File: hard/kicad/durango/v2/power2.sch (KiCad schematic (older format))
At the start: 71 parts, among them J11 EXPANSION, J4 LED, J605 COMPONENT VIDEO, J7 POWER IN, J706 COMPOSITE, J8 DEBUG, J9 CARTRIDGE, Q608 BC548, Q609 BC548, Q610 BC548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

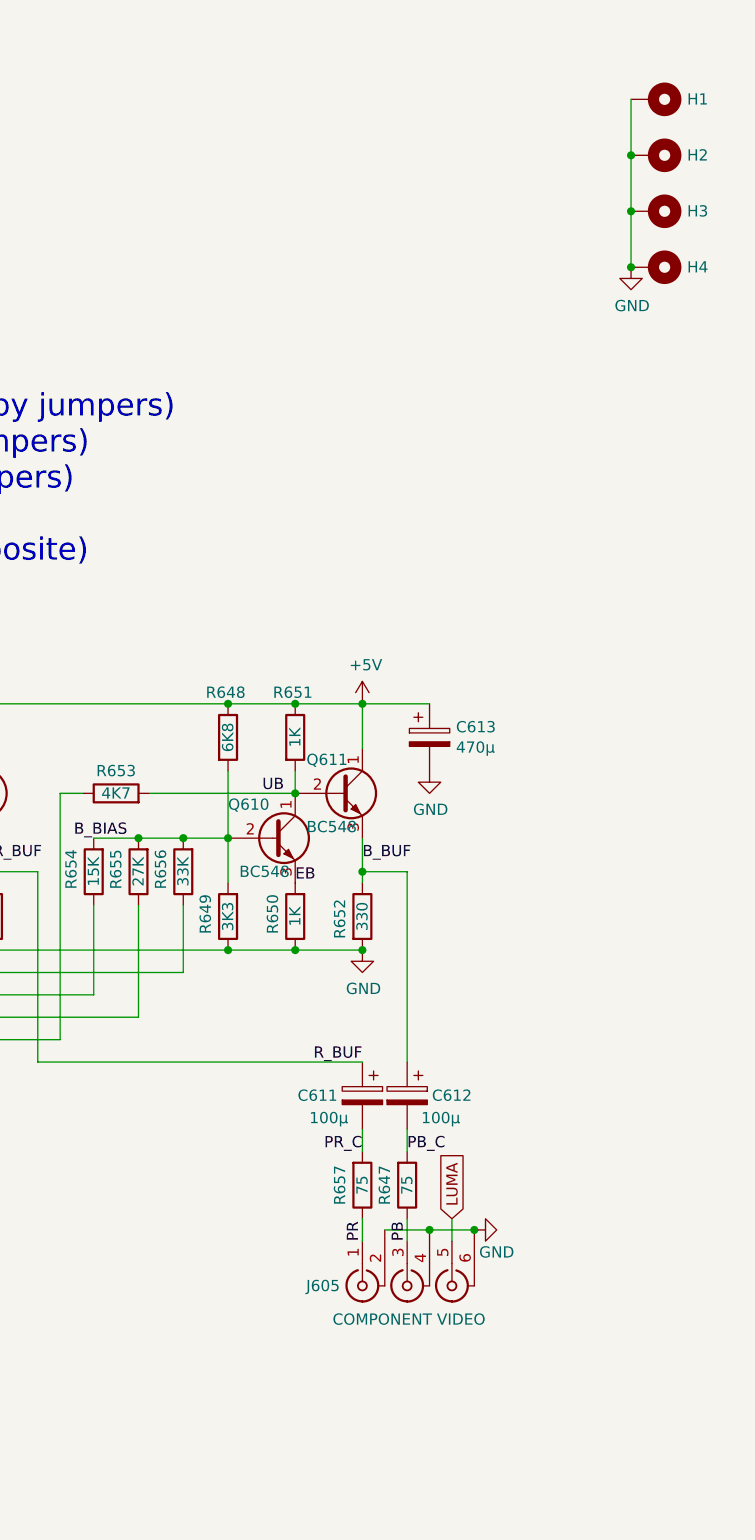
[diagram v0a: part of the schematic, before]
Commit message: add narrow SRAM footprint
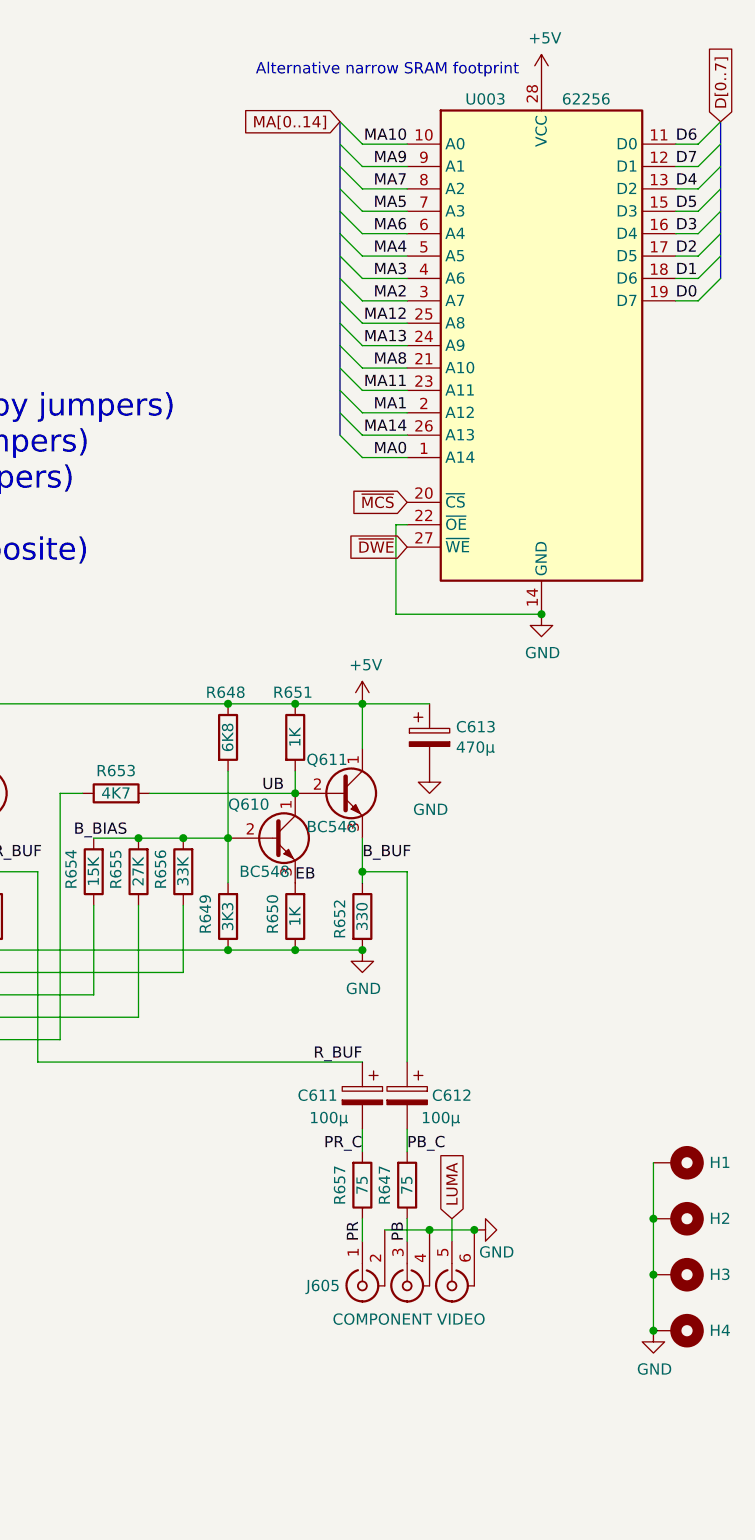
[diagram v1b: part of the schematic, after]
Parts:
- added U003: 62256, Package_DIP:DIP-28_W7.62mm_Socket, symbol 62256:62256
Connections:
- net +5V: now also U003.28 (VCC)
- net D0: now also U003.19 (D7)
- net D1: now also U003.18 (D6)
- net D2: now also U003.17 (D5)
- net D3: now also U003.16 (D4)
- net D4: now also U003.13 (D2)
- net D5: now also U003.15 (D3)
- net D6: now also U003.11 (D0)
- net D7: now also U003.12 (D1)
- net GND: now also U003.14 (GND), U003.22 (~OE~)
- new net MA0: U003.1 (A14)
- new net MA1: U003.2 (A12)
- new net MA10: U003.10 (A0)
- new net MA11: U003.23 (A11)
- new net MA12: U003.25 (A8)
- new net MA13: U003.24 (A9)
- new net MA14: U003.26 (A13)
- new net MA2: U003.3 (A7)
- new net MA3: U003.4 (A6)
- new net MA4: U003.5 (A5)
- new net MA5: U003.7 (A3)
- new net MA6: U003.6 (A4)
- new net MA7: U003.8 (A2)
- new net MA8: U003.21 (A10)
- new net MA9: U003.9 (A1)
- new net ~DWE: U003.27 (~WE~)
- new net ~MCS: U003.20 (~CS)
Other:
- note added: "Alternative narrow SRAM footprint"
- moved on the sheet: H1, H2, H3, H4

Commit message: fix CCIR v2.2
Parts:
- JP3: value SWITCH -> POWER
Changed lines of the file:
@@
 P 2600 6500
 F 0 "R32" H 2670 6546 50  0000 L CNN
-F 1 "1K" V 2600 6450 50  0000 L CNN
+F 1 "1K" V 2600 6450 50  0000 L CIN
 F 2 "Resistor_THT:R_Axial_DIN0207_L6.3mm_D2.5mm_P2.54mm_Vertical" V 2530 6500 50  0001 C CNN
 F 3 "~" H 2600 6500 50  0001 C CNN
@@
 P 1400 800
 F 0 "JP3" V 1250 600 50  0000 L CNN
-F 1 "SWITCH" H 1300 900 50  0000 L CNN
+F 1 "POWER" H 1300 900 50  0000 L CNN
 F 2 "durango:PowerSwitch" H 1400 800 50  0001 C CNN
 F 3 "~" H 1400 800 50  0001 C CNN

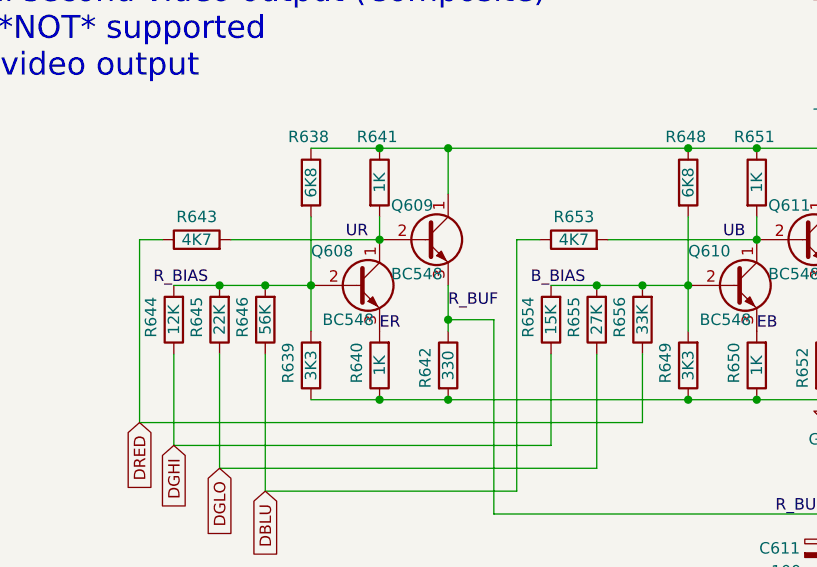
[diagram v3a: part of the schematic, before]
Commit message: fix YUV output values on silkscreen
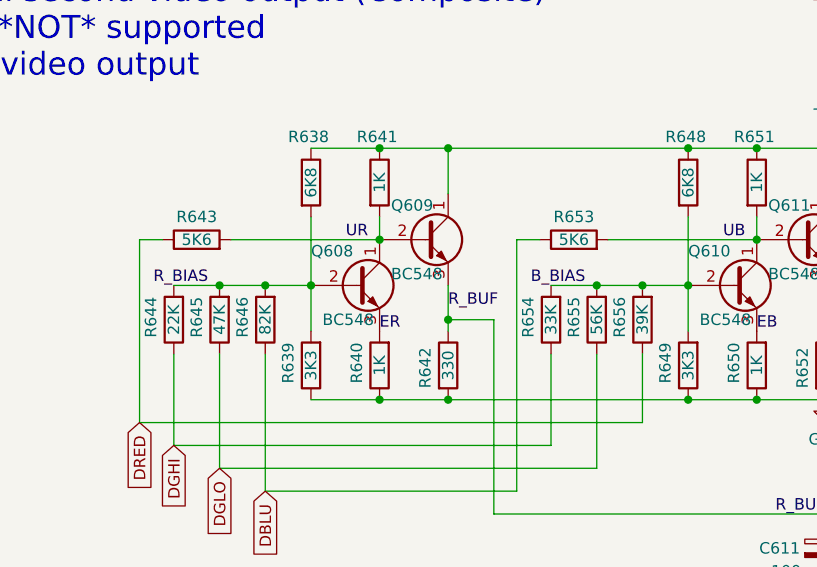
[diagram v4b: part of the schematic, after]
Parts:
- R643, R653: value 4K7 -> 5K6
- R644: value 12K -> 22K
- R645: value 22K -> 47K
- R646: value 56K -> 82K
- R654: value 15K -> 33K
- R655: value 27K -> 56K
- R656: value 33K -> 39K
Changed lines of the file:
@@
 P 7050 4250
 F 0 "R646" V 7150 4150 50  0000 L CNN
-F 1 "56K" V 7050 4250 50  0000 C CNN
+F 1 "82K" V 7050 4250 50  0000 C CNN
 F 2 "Resistor_THT:R_Axial_DIN0207_L6.3mm_D2.5mm_P2.54mm_Vertical" V 6980 4250 50  0001 C CNN
 F 3 "~" H 7050 4250 50  0001 C CNN
@@
 P 6850 4250
 F 0 "R645" V 6950 4150 50  0000 L CNN
-F 1 "22K" V 6850 4250 50  0000 C CNN
+F 1 "47K" V 6850 4250 50  0000 C CNN
 F 2 "Resistor_THT:R_Axial_DIN0207_L6.3mm_D2.5mm_P2.54mm_Vertical" V 6780 4250 50  0001 C CNN
 F 3 "~" H 6850 4250 50  0001 C CNN
@@
 P 6650 4250
 F 0 "R644" V 6750 4150 50  0000 L CNN
-F 1 "12K" V 6650 4250 50  0000 C CNN
+F 1 "22K" V 6650 4250 50  0000 C CNN
 F 2 "Resistor_THT:R_Axial_DIN0207_L6.3mm_D2.5mm_P2.54mm_Vertical" V 6580 4250 50  0001 C CNN
 F 3 "~" H 6650 4250 50  0001 C CNN
@@
 P 6750 3900
 F 0 "R643" V 6850 3900 50  0000 C CNN
-F 1 "4K7" V 6750 3900 50  0000 C CNN
+F 1 "5K6" V 6750 3900 50  0000 C CNN
 F 2 "Resistor_THT:R_Axial_DIN0207_L6.3mm_D2.5mm_P2.54mm_Vertical" V 6680 3900 50  0001 C CNN
 F 3 "~" H 6750 3900 50  0001 C CNN
@@
 P 8700 4250
 F 0 "R656" V 8800 4150 50  0000 L CNN
-F 1 "33K" V 8700 4250 50  0000 C CNN
+F 1 "39K" V 8700 4250 50  0000 C CNN
 F 2 "Resistor_THT:R_Axial_DIN0207_L6.3mm_D2.5mm_P2.54mm_Vertical" V 8630 4250 50  0001 C CNN
 F 3 "~" H 8700 4250 50  0001 C CNN
@@
 P 8500 4250
 F 0 "R655" V 8600 4150 50  0000 L CNN
-F 1 "27K" V 8500 4250 50  0000 C CNN
+F 1 "56K" V 8500 4250 50  0000 C CNN
 F 2 "Resistor_THT:R_Axial_DIN0207_L6.3mm_D2.5mm_P2.54mm_Vertical" V 8430 4250 50  0001 C CNN
 F 3 "~" H 8500 4250 50  0001 C CNN
@@
 P 8300 4250
 F 0 "R654" V 8400 4150 50  0000 L CNN
-F 1 "15K" V 8300 4250 50  0000 C CNN
+F 1 "33K" V 8300 4250 50  0000 C CNN
 F 2 "Resistor_THT:R_Axial_DIN0207_L6.3mm_D2.5mm_P2.54mm_Vertical" V 8230 4250 50  0001 C CNN
 F 3 "~" H 8300 4250 50  0001 C CNN
@@
 P 8400 3900
 F 0 "R653" V 8500 3900 50  0000 C CNN
-F 1 "4K7" V 8400 3900 50  0000 C CNN
+F 1 "5K6" V 8400 3900 50  0000 C CNN
 F 2 "Resistor_THT:R_Axial_DIN0207_L6.3mm_D2.5mm_P2.54mm_Vertical" V 8330 3900 50  0001 C CNN
 F 3 "~" H 8400 3900 50  0001 C CNN

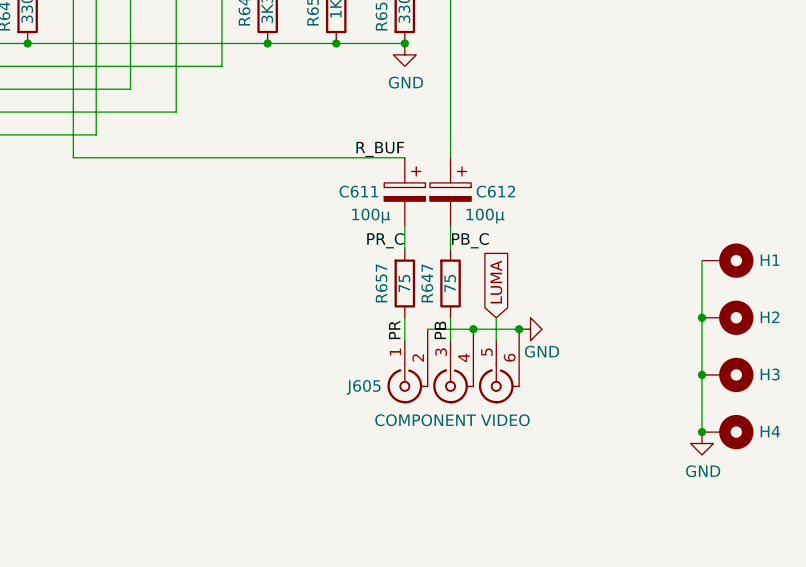
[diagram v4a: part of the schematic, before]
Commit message: fix YUV output silkscreen
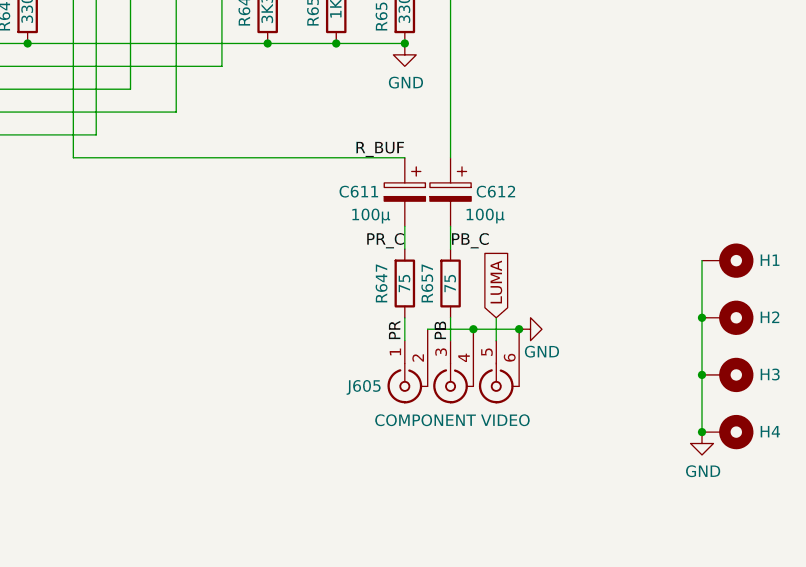
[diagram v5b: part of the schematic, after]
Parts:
- renumbered R657 to R647, R647 to R657
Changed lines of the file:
@@
 $EndComp
 $Comp
-L Device:R R657
+L Device:R R647
 U 1 1 65030F60
 P 9500 5650
-F 0 "R657" V 9400 5650 50  0000 C CNN
+F 0 "R647" V 9400 5650 50  0000 C CNN
 F 1 "75" V 9500 5650 50  0000 C CNN
 F 2 "Resistor_THT:R_Axial_DIN0207_L6.3mm_D2.5mm_P2.54mm_Vertical" V 9430 5650 50  0001 C CNN
@@
 $EndComp
 $Comp
-L Device:R R647
+L Device:R R657
 U 1 1 65031F66
 P 9700 5650
-F 0 "R647" V 9600 5650 50  0000 C CNN
+F 0 "R657" V 9600 5650 50  0000 C CNN
 F 1 "75" V 9700 5650 50  0000 C CNN
 F 2 "Resistor_THT:R_Axial_DIN0207_L6.3mm_D2.5mm_P2.54mm_Vertical" V 9630 5650 50  0001 C CNN
